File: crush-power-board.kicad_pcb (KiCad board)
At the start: 4 copper layers, 101.6 x 120.6 mm, 109 parts, among them J1 XT90PW-F, J2 1x2 Header, J3 Molex Micro Fit 3.0, J4 Barrel_Jack, J5 2157601008, U1 BD9G341AEFJ, U2 SIC461ED-T1-GE3, U3 SIC461ED-T1-GE3, U4 BD9G341AEFJ

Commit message: cleanup traces/vias
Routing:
- net 12V: track 212.4 -> 172.7 mm
- net +BATT: track 149.8 -> 140.5 mm
- net 5V: vias 227 -> 218
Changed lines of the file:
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@@
   (segment (start 60.7 79.1) (end 46.6 79.1) (width 0.35) (layer "In2.Cu") (net 1))
   (segment (start 60.7 89) (end 60.7 79.1) (width 0.35) (layer "In2.Cu") (net 1))
+  (segment (start 23.3 111.125) (end 24.65 111.125) (width 0.35) (layer "B.Cu") (net 1))
   (segment (start 66.387653 68.887653) (end 66.3 68.975306) (width 0.35) (layer "B.Cu") (net 1))
-  (segment (start 23.3 111.125) (end 24.65 111.125) (width 0.35) (layer "B.Cu") (net 1))
-  (segment (start 30.2 105.575) (end 30.2 74.775) (width 0.35) (layer "B.Cu") (net 1))
+  (segment (start 24.65 111.125) (end 30.2 105.575) (width 0.35) (layer "B.Cu") (net 1))
   (segment (start 79.7 75.9) (end 81.2 74.4) (width 0.35) (layer "B.Cu") (net 1))
-  (segment (start 24.65 111.125) (end 30.2 105.575) (width 0.35) (layer "B.Cu") (net 1))
+  (segment (start 30.2 105.575) (end 30.2 84) (width 0.35) (layer "B.Cu") (net 1))
   (segment (start 67.225306 68.05) (end 66.387653 68.887653) (width 0.35) (layer "B.Cu") (net 1))
   (segment (start 100.4322 93.5) (end 100.5266 93.5944) (width 0.35) (layer "B.Cu") (net 1))
@@
   (segment (start 63.9 75.9) (end 79.7 75.9) (width 0.35) (layer "B.Cu") (net 1))
   (segment (start 81.2 74.4) (end 81.2 73.1) (width 0.35) (layer "B.Cu") (net 1))
+  (segment (start 35.1 79.1) (end 46.6 79.1) (width 0.35) (layer "B.Cu") (net 1))
   (segment (start 68.3 68.05) (end 67.225306 68.05) (width 0.35) (layer "B.Cu") (net 1))
   (segment (start 98.5 93.5) (end 100.4322 93.5) (width 0.35) (layer "B.Cu") (net 1))
-  (segment (start 35.3 79.1) (end 46.6 79.1) (width 0.35) (layer "B.Cu") (net 1))
-  (segment (start 30.2 84.2) (end 35.3 79.1) (width 0.35) (layer "B.Cu") (net 1))
+  (segment (start 30.2 84) (end 35.1 79.1) (width 0.35) (layer "B.Cu") (net 1))
   (segment (start 68.725 62.755) (end 68.725 60.725) (width 0.25) (layer "F.Cu") (net 2))
   (segment (start 68.075 60.125) (end 68.1 60.1) (width 0.35) (layer "F.Cu") (net 2))
@@
   (via (at 97.1804 31.6992) (size 0.8) (drill 0.4) (layers "F.Cu" "B.Cu") (free) (net 16))
   (segment (start 52.3 80) (end 52.3 74.2) (width 0.25) (layer "In1.Cu") (net 16))
-  (segment (start 47.325 79.400305) (end 47.325 78.799695) (width 0.25) (layer "B.Cu") (net 16))
-  (segment (start 38.105 88.620305) (end 47.325 79.400305) (width 0.25) (layer "B.Cu") (net 16))
-  (segment (start 32.600305 94.01) (end 37.680305 94.01) (width 0.25) (layer "B.Cu") (net 16))
   (segment (start 30.5 107.5) (end 31 107) (width 0.25) (layer "B.Cu") (net 16))
-  (segment (start 35.9 80) (end 52.3 80) (width 0.25) (layer "B.Cu") (net 16))
+  (segment (start 31 107) (end 31 95.725306) (width 0.25) (layer "B.Cu") (net 16))
+  (segment (start 46.725306 80) (end 52.3 80) (width 0.25) (layer "B.Cu") (net 16))
   (segment (start 62.15 58.75) (end 61.5 59.4) (width 0.25) (layer "B.Cu") (net 16))
-  (segment (start 37.680305 94.01) (end 38.105 93.585305) (width 0.25) (layer "B.Cu") (net 16))
   (segment (start 52.3 37.8) (end 53 37.1) (width 0.25) (layer "B.Cu") (net 16))
-  (segment (start 31.1 84.8) (end 35.9 80) (width 0.25) (layer "B.Cu") (net 16))
   (segment (start 62.15 43.55) (end 62.15 58.75) (width 0.25) (layer "B.Cu") (net 16))
-  (segment (start 31 107) (end 31 95.610305) (width 0.25) (layer "B.Cu") (net 16))
-  (segment (start 38.105 93.585305) (end 38.105 88.620305) (width 0.25) (layer "B.Cu") (net 16))
   (segment (start 53 37.1) (end 68.6 37.1) (width 0.25) (layer "B.Cu") (net 16))
   (segment (start 52.3 74.2) (end 52.3 74.4) (width 0.25) (layer "B.Cu") (net 16))
-  (segment (start 31 95.610305) (end 32.600305 94.01) (width 0.25) (layer "B.Cu") (net 16))
   (segment (start 68.6 37.1) (end 62.15 43.55) (width 0.25) (layer "B.Cu") (net 16))
+  (segment (start 31 95.725306) (end 46.725306 80) (width 0.25) (layer "B.Cu") (net 16))
   (segment (start 52.3 74.2) (end 52.3 37.8) (width 0.25) (layer "B.Cu") (net 16))
-  (segment (start 47.325 78.799695) (end 43.900305 75.375) (width 0.25) (layer "B.Cu") (net 16))
   (segment (start 68.6 37.1) (end 85.2 20.5) (width 0.25) (layer "B.Cu") (net 16))
-  (segment (start 43.900305 75.375) (end 31.1 75.375) (width 0.25) (layer "B.Cu") (net 16))
   (segment (start 101.9266 94.3944) (end 101.7956 94.3944) (width 0.25) (layer "F.Cu") (net 17))
   (segment (start 103.3956 92.7944) (end 101.9266 94.2634) (width 0.35) (layer "F.Cu") (net 17))
@@
   (via (at 66.83 111.77) (size 0.8) (drill 0.4) (layers "F.Cu" "B.Cu") (free) (net 25))
   (via (at 75.41 119.23) (size 0.8) (drill 0.4) (layers "F.Cu" "B.Cu") (free) (net 25))
-  (via (at 33.57 80.585) (size 0.8) (drill 0.4) (layers "F.Cu" "B.Cu") (free) (net 25))
   (via (at 84.54 124.37) (size 0.8) (drill 0.4) (layers "F.Cu" "B.Cu") (free) (net 25))
   (via (at 85.81 123.1) (size 0.8) (drill 0.4) (layers "F.Cu" "B.Cu") (free) (net 25))
@@
   (via (at 66.83 97.8) (size 0.8) (drill 0.4) (layers "F.Cu" "B.Cu") (free) (net 25))
   (via (at 68.1 105.42) (size 0.8) (drill 0.4) (layers "F.Cu" "B.Cu") (free) (net 25))
-  (via (at 37.38 89.475) (size 0.8) (drill 0.4) (layers "F.Cu" "B.Cu") (free) (net 25))
   (via (at 67.7 124.3) (size 0.8) (drill 0.4) (layers "F.Cu" "B.Cu") (free) (net 25))
   (via (at 66.83 105.42) (size 0.8) (drill 0.4) (layers "F.Cu" "B.Cu") (free) (net 25))
   (via (at 33.57 90.745) (size 0.8) (drill 0.4) (layers "F.Cu" "B.Cu") (free) (net 25))
-  (via (at 34.84 92.015) (size 0.8) (drill 0.4) (layers "F.Cu" "B.Cu") (free) (net 25))
   (via (at 33.57 78.045) (size 0.8) (drill 0.4) (layers "F.Cu" "B.Cu") (free) (net 25))
   (via (at 33.57 100.905) (size 0.8) (drill 0.4) (layers "F.Cu" "B.Cu") (free) (net 25))
   (via (at 37.38 93.285) (size 0.8) (drill 0.4) (layers "F.Cu" "B.Cu") (free) (net 25))
-  (via (at 36.11 90.745) (size 0.8) (drill 0.4) (layers "F.Cu" "B.Cu") (free) (net 25))
   (via (at 36.11 100.905) (size 0.8) (drill 0.4) (layers "F.Cu" "B.Cu") (free) (net 25))
   (via (at 77.95 120.5) (size 0.8) (drill 0.4) (layers "F.Cu" "B.Cu") (free) (net 25))
   (via (at 36.11 95.825) (size 0.8) (drill 0.4) (layers "F.Cu" "B.Cu") (free) (net 25))
-  (via (at 33.57 93.285) (size 0.8) (drill 0.4) (layers "F.Cu" "B.Cu") (free) (net 25))
   (via (at 66.83 88.91) (size 0.8) (drill 0.4) (layers "F.Cu" "B.Cu") (free) (net 25))
   (via (at 72.87 121.77) (size 0.8) (drill 0.4) (layers "F.Cu" "B.Cu") (free) (net 25))
@@
   (via (at 71.6 123.04) (size 0.8) (drill 0.4) (layers "F.Cu" "B.Cu") (free) (net 25))
   (via (at 66.83 90.18) (size 0.8) (drill 0.4) (layers "F.Cu" "B.Cu") (free) (net 25))
-  (via (at 32.3 81.855) (size 0.8) (drill 0.4) (layers "F.Cu" "B.Cu") (free) (net 25))
   (via (at 68.1 111.77) (size 0.8) (drill 0.4) (layers "F.Cu" "B.Cu") (free) (net 25))
   (via (at 32.3 100.905) (size 0.8) (drill 0.4) (layers "F.Cu" "B.Cu") (free) (net 25))
   (via (at 66.83 93.99) (size 0.8) (drill 0.4) (layers "F.Cu" "B.Cu") (free) (net 25))
-  (via (at 37.38 79.315) (size 0.8) (drill 0.4) (layers "F.Cu" "B.Cu") (free) (net 25))
   (via (at 32.3 90.745) (size 0.8) (drill 0.4) (layers "F.Cu" "B.Cu") (free) (net 25))
   (via (at 34.84 95.825) (size 0.8) (drill 0.4) (layers "F.Cu" "B.Cu") (free) (net 25))
@@
   (via (at 34.84 78.045) (size 0.8) (drill 0.4) (layers "F.Cu" "B.Cu") (free) (net 25))
   (via (at 33.57 76.775) (size 0.8) (drill 0.4) (layers "F.Cu" "B.Cu") (free) (net 25))
-  (via (at 34.84 79.315) (size 0.8) (drill 0.4) (layers "F.Cu" "B.Cu") (free) (net 25))
   (via (at 32.3 89.475) (size 0.8) (drill 0.4) (layers "F.Cu" "B.Cu") (free) (net 25))
   (via (at 37.38 105.985) (size 0.8) (drill 0.4) (layers "F.Cu" "B.Cu") (free) (net 25))
-  (via (at 36.11 79.315) (size 0.8) (drill 0.4) (layers "F.Cu" "B.Cu") (free) (net 25))
   (via (at 33.57 86.935) (size 0.8) (drill 0.4) (layers "F.Cu" "B.Cu") (free) (net 25))
   (via (at 68.1 101.61) (size 0.8) (drill 0.4) (layers "F.Cu" "B.Cu") (free) (net 25))

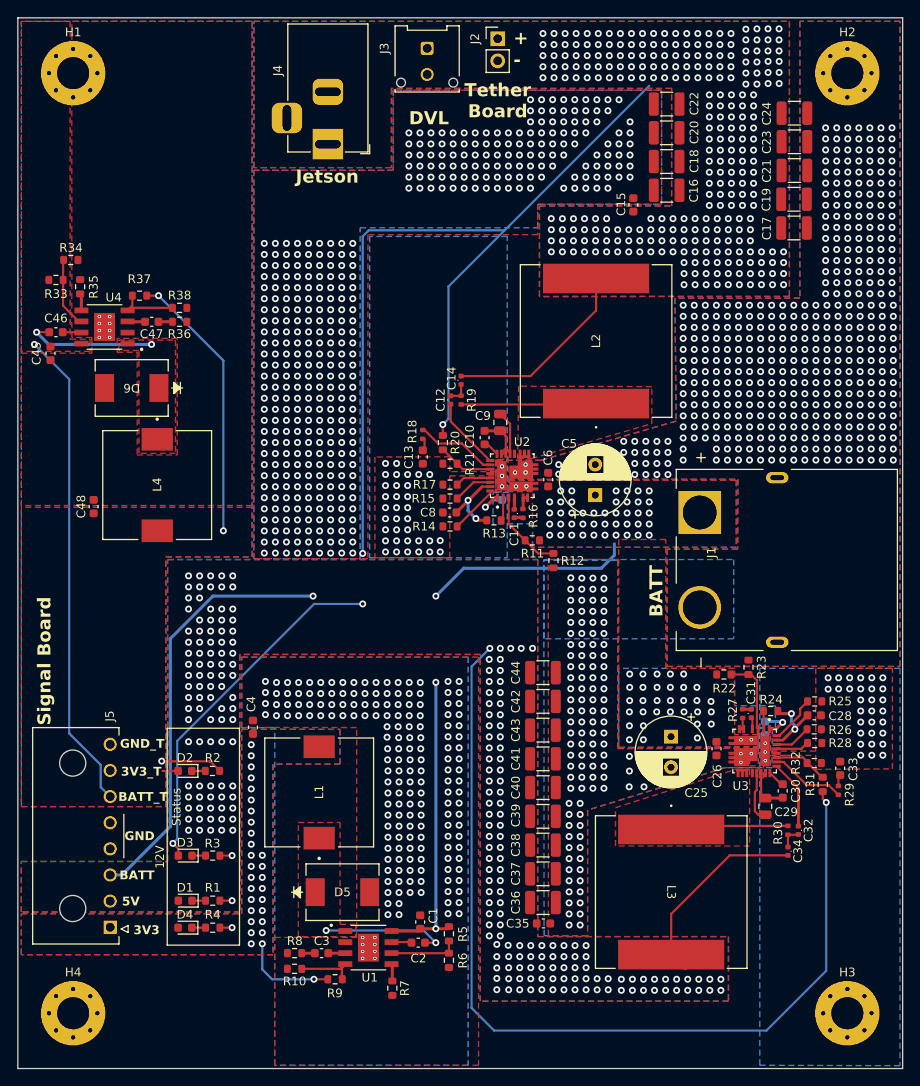
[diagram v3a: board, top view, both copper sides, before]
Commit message: Silkscreen changes
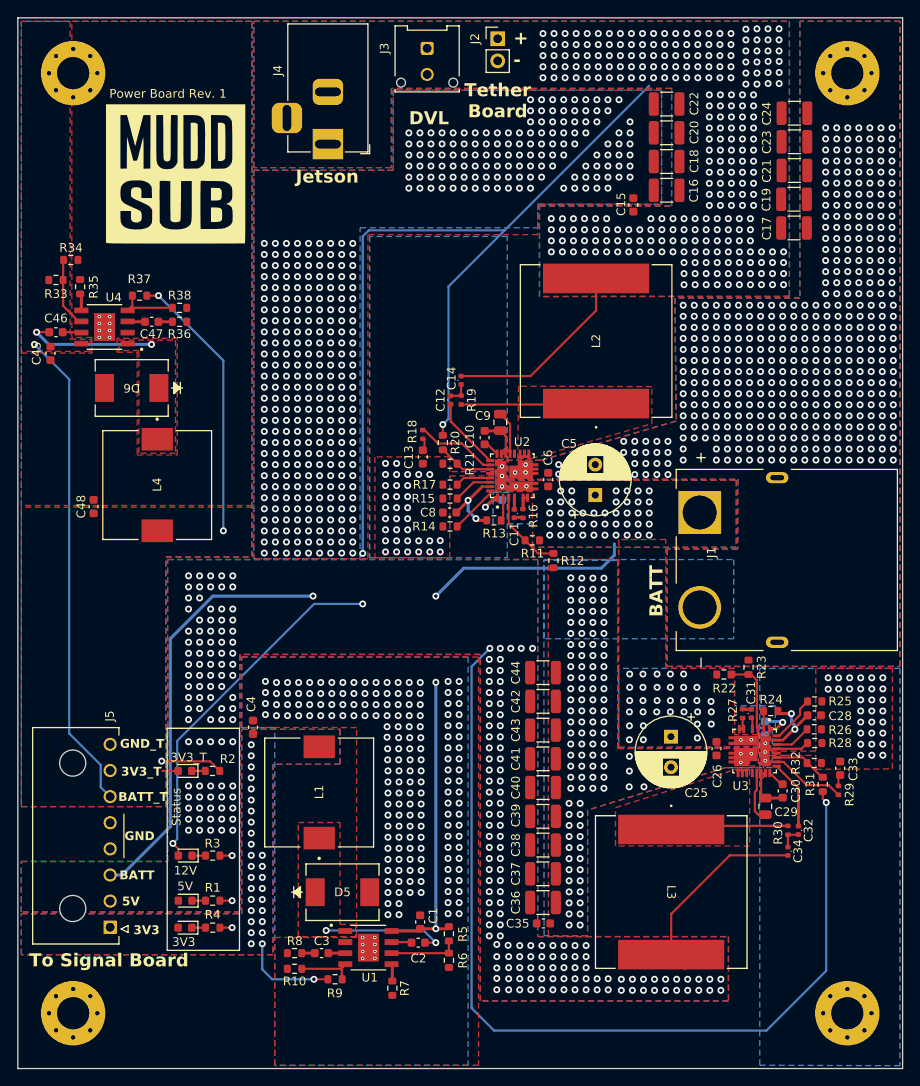
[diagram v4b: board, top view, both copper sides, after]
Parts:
- added G***: LOGO, LOGO, F.Cu at (30.8, 30.6)
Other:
- board text added: "Power Board Rev. 1"
- board text added: "To Signal Board"
- board text removed: "Signal Board"

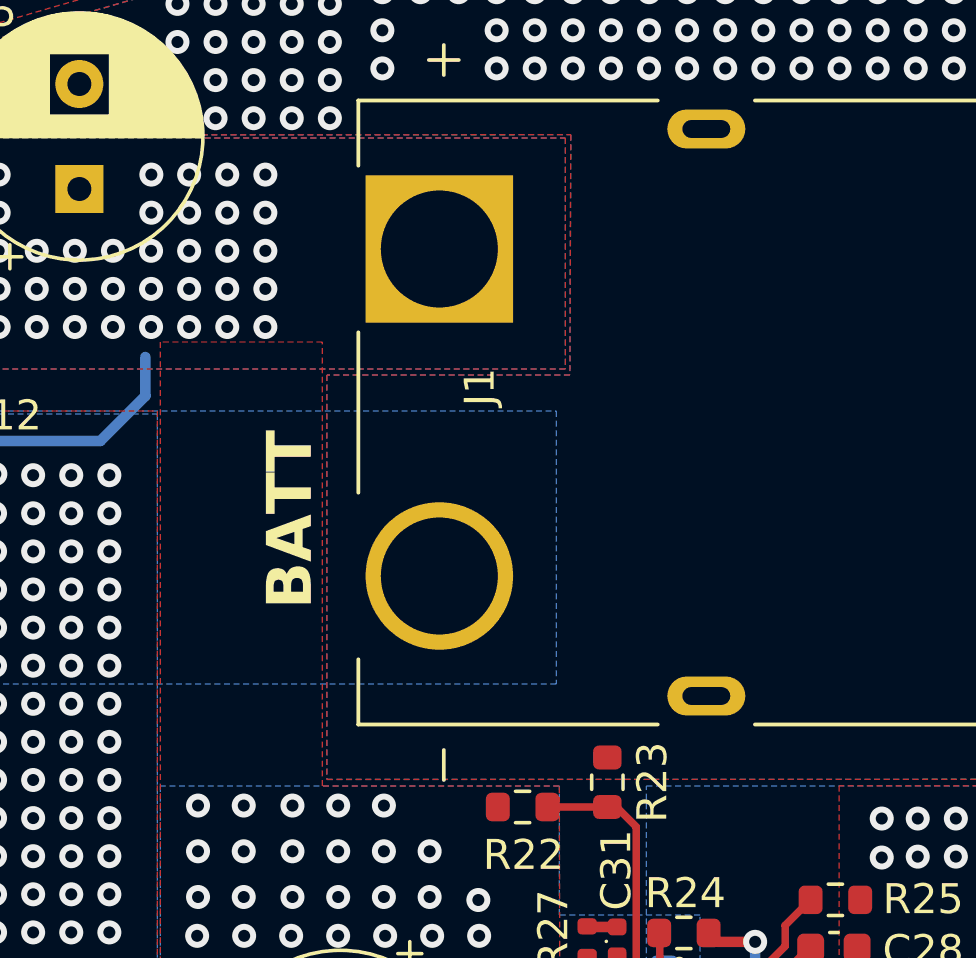
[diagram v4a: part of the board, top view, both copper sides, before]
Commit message: added JLC order number placement
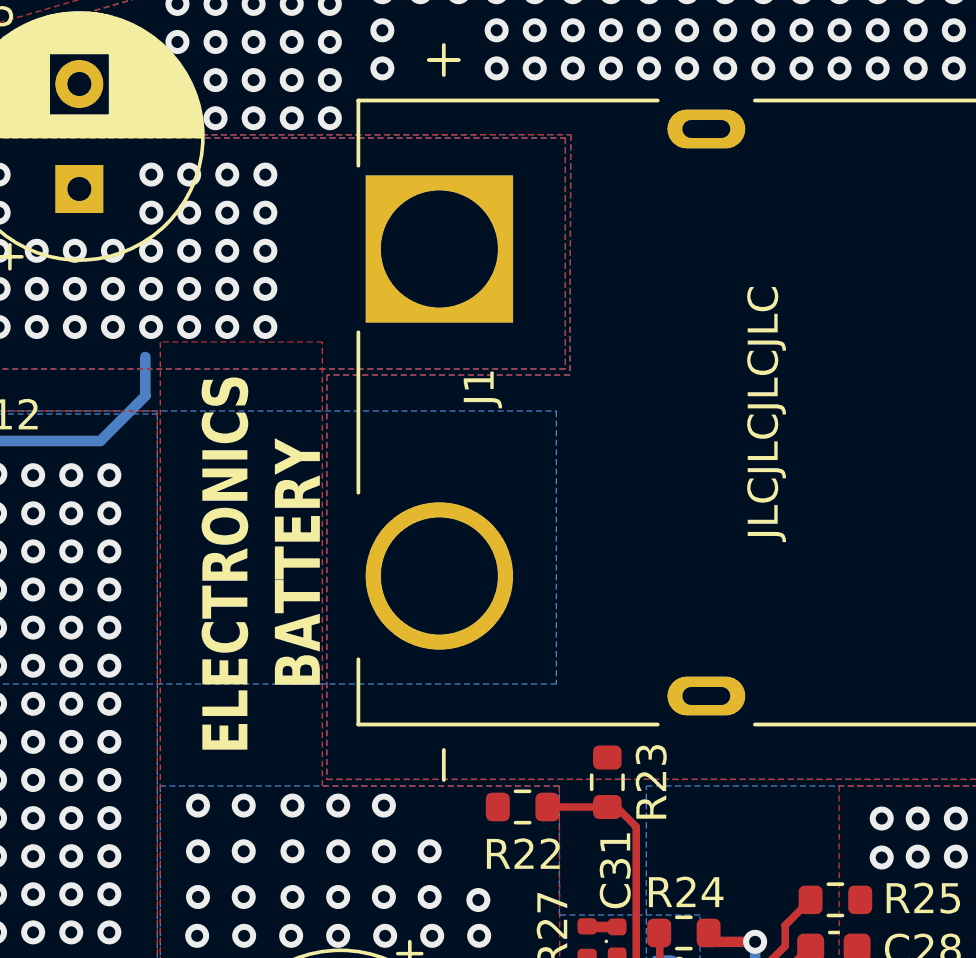
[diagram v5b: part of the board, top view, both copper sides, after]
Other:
- board text added: "ELECTRONICS BATTERY"
- board text added: "JLCJLCJLCJLC"
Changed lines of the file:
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@@
     (effects (font (size 1.5 1.5) (thickness 0.3) bold) (justify left bottom))
+  )
+  (gr_text "JLCJLCJLCJLC" (at 102.4 79.2 90) (layer "F.SilkS")
+    (effects (font (size 1 1) (thickness 0.15)) (justify left bottom))
   )
   (gr_text "12V" (at 30.6 111.2) (layer "F.SilkS")
@@
     (effects (font (size 1.016 1.016) (thickness 0.150012) bold))
   )
-  (gr_text "BATT" (at 86.9 81.5 90) (layer "F.SilkS")
-    (effects (font (size 1.5 1.5) (thickness 0.3) bold) (justify left bottom))
+  (gr_text "ELECTRONICS\nBATTERY" (at 87.2 80 90) (layer "F.SilkS")
+    (effects (font (size 1.5 1.2) (thickness 0.3) bold) (justify bottom))
   )
   (gr_text "+" (at 69.6 15.9) (layer "F.SilkS")

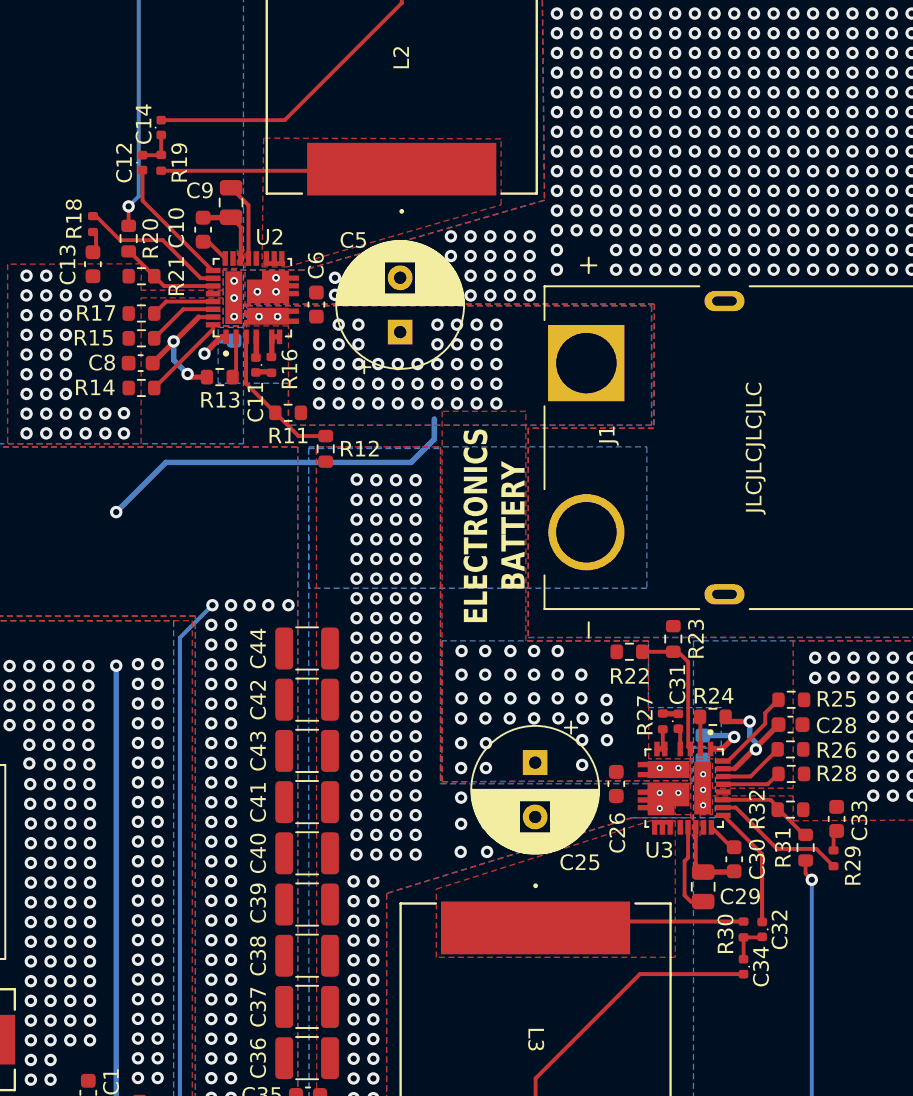
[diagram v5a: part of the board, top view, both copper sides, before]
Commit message: use 4u7 capacitors for vsns pins
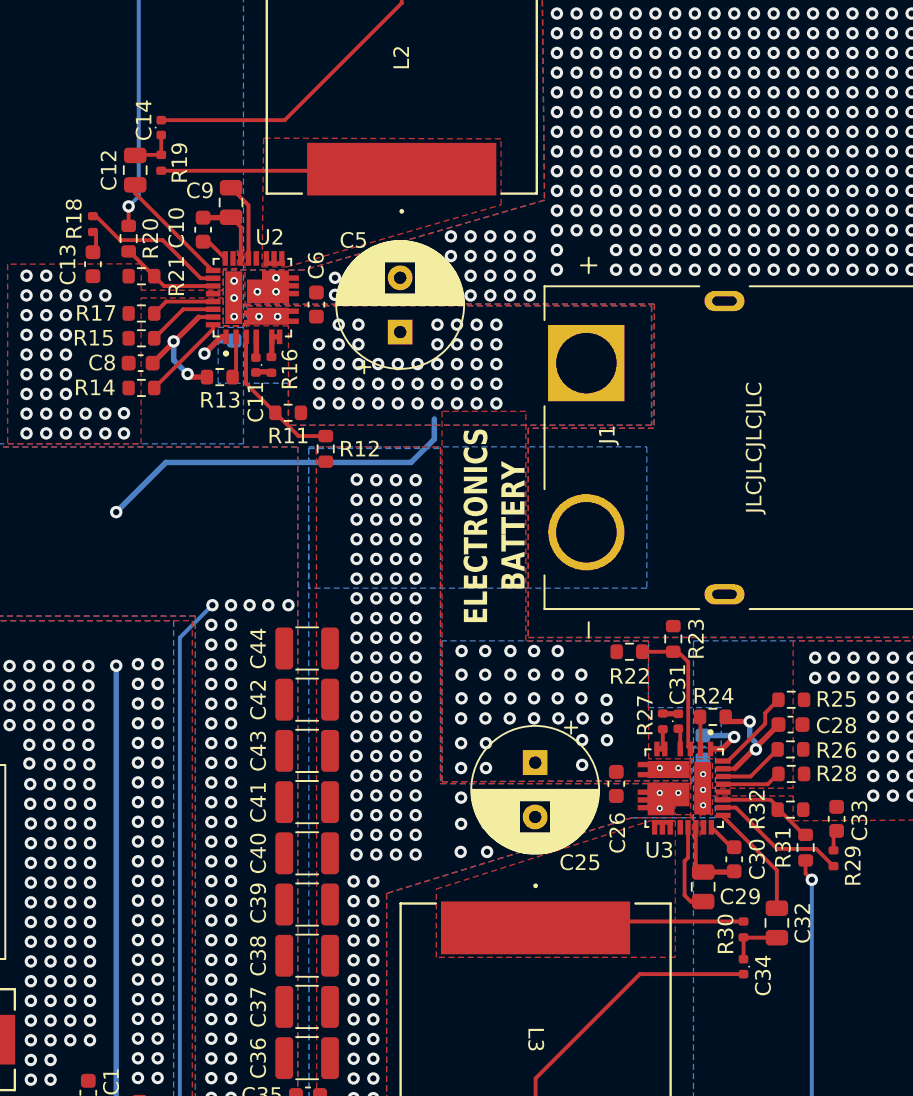
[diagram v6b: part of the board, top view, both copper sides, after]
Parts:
- C12, C32: value 3u9 -> 4u7; footprint crush-power-footprints:C_0402_1005Metric -> Capacitor_SMD:C_0805_2012Metric
- moved C32 1.04 mm to (103.3, 105.6)
- moved C12 0.68 mm to (61.9, 57.1)
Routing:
- net Net-(U3-VSNS): track 12.3 -> 7.42 mm
- net Net-(C32-Pad2): track 2.62 -> 3.57 mm
- net Net-(U2-VSNS): track 8.39 -> 7.63 mm
- net Net-(C12-Pad2): track 2.49 -> 3.00 mm
